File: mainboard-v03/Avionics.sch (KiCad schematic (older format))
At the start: 42 parts, among them J10 Conn_01x03, J8 Conn_01x09, J9 Conn_01x05, SW1 KMR231NG LFS, U1 MAX706RS-T, U2 ATSAMD51J20A-AU, U3 LSM9DS1, Y1 32.768kHz

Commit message: schematic organizing
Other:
- moved on the sheet: J10, J8, J9
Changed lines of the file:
@@
 Text GLabel 4600 5850 0    50   BiDi ~ 0
 PA19
-Text GLabel 1500 5150 2    59   BiDi ~ 0
+Text GLabel 10050 1600 2    59   BiDi ~ 0
 MOSI
-Text GLabel 1500 5050 2    59   BiDi ~ 0
+Text GLabel 10050 1500 2    59   BiDi ~ 0
 SCK
-Text GLabel 1500 5250 2    59   BiDi ~ 0
+Text GLabel 10050 1700 2    59   BiDi ~ 0
 MISO
 Wire Wire Line
-	1500 5150 1400 5150
-Wire Wire Line
-	1500 5050 1400 5050
-Wire Wire Line
-	1500 5250 1400 5250
+	10050 1600 9950 1600
+Wire Wire Line
+	10050 1500 9950 1500
+Wire Wire Line
+	10050 1700 9950 1700
 Wire Wire Line
 	6050 4850 5900 4850
@@
 	3350 1300 3150 1300
 Wire Wire Line
-	1400 5550 1500 5550
-Text GLabel 1500 5550 2    50   BiDi ~ 0
+	9950 2000 10050 2000
+Text GLabel 10050 2000 2    50   BiDi ~ 0
 PA20
 Wire Wire Line
-	1400 5650 1500 5650
-Text GLabel 1500 5650 2    50   BiDi ~ 0
+	9950 2100 10050 2100
+Text GLabel 10050 2100 2    50   BiDi ~ 0
 PA22
 Wire Wire Line
-	1400 5350 1500 5350
-Text GLabel 1500 5350 2    50   BiDi ~ 0
+	9950 1800 10050 1800
+Text GLabel 10050 1800 2    50   BiDi ~ 0
 PB23
 Wire Wire Line
-	1400 5450 1500 5450
-Text GLabel 1500 5450 2    50   BiDi ~ 0
+	9950 1900 10050 1900
+Text GLabel 10050 1900 2    50   BiDi ~ 0
 PB22
 $Comp
 L Connector_Generic:Conn_01x09 J8
 U 1 1 5D3643AA
-P 1200 5250
-F 0 "J8" H 1118 5775 50  0000 C CNN
-F 1 "Conn_01x09" H 1118 5776 50  0001 C CNN
-F 2 "Connector_PinHeader_2.54mm:PinHeader_1x09_P2.54mm_Vertical" H 1200 5250 50  0001 C CNN
-F 3 "~" H 1200 5250 50  0001 C CNN
-	1    1200 5250
+P 9750 1700
+F 0 "J8" H 9668 2225 50  0000 C CNN
+F 1 "Conn_01x09" H 9668 2226 50  0001 C CNN
+F 2 "Connector_PinHeader_2.54mm:PinHeader_1x09_P2.54mm_Vertical" H 9750 1700 50  0001 C CNN
+F 3 "~" H 9750 1700 50  0001 C CNN
+	1    9750 1700
 	-1   0    0    -1
 $EndComp
@@
 L mainboard:3.3V #SUPPLY?
 U 1 0 5D370A56
-P 1950 4850
+P 10500 1300
 AR Path="/5D370A56" Ref="#SUPPLY?"  Part="1"
 AR Path="/5CEC5A72/5D370A56" Ref="#SUPPLY0111"  Part="1"
-F 0 "#SUPPLY0111" H 1950 4850 50  0001 C CNN
-F 1 "3.3V" H 1910 4990 59  0000 L BNN
-F 2 "" H 1950 4850 50  0001 C CNN
-F 3 "" H 1950 4850 50  0001 C CNN
-	1    1950 4850
+F 0 "#SUPPLY0111" H 10500 1300 50  0001 C CNN
+F 1 "3.3V" H 10460 1440 59  0000 L BNN
+F 2 "" H 10500 1300 50  0001 C CNN
+F 3 "" H 10500 1300 50  0001 C CNN
+	1    10500 1300
 	-1   0    0    -1
 $EndComp
@@
 L mainboard:GND #GND?
 U 1 0 5D3722F9
-P 1950 5050
+P 10500 1500
 AR Path="/5D3722F9" Ref="#GND?"  Part="1"
 AR Path="/5CEC5A72/5D3722F9" Ref="#GND0101"  Part="1"
-F 0 "#GND0101" H 1950 5050 50  0001 C CNN
-F 1 "GND" H 1850 4950 59  0000 L BNN
-F 2 "" H 1950 5050 50  0001 C CNN
-F 3 "" H 1950 5050 50  0001 C CNN
-	1    1950 5050
+F 0 "#GND0101" H 10500 1500 50  0001 C CNN
+F 1 "GND" H 10400 1400 59  0000 L BNN
+F 2 "" H 10500 1500 50  0001 C CNN
+F 3 "" H 10500 1500 50  0001 C CNN
+	1    10500 1500
 	1    0    0    -1
 $EndComp
 Wire Wire Line
-	1400 4950 1950 4950
-Wire Wire Line
-	1950 4850 1400 4850
+	9950 1400 10500 1400
+Wire Wire Line
+	10500 1300 9950 1300
 Wire Wire Line
 	4700 4150 4600 4150
@@
 L Connector_Generic:Conn_01x05 J9
 U 1 1 5D408200
-P 1150 6550
-F 0 "J9" H 1068 6967 50  0000 C CNN
-F 1 "Conn_01x05" V 1068 6876 50  0001 C CNN
-F 2 "Connector_PinHeader_2.54mm:PinHeader_1x05_P2.54mm_Vertical" H 1150 6550 50  0001 C CNN
-F 3 "~" H 1150 6550 50  0001 C CNN
-	1    1150 6550
-	-1   0    0    -1
-$EndComp
-Wire Wire Line
-	1350 6350 1450 6350
-Text GLabel 1450 6350 2    50   BiDi ~ 0
+P 9700 3000
+F 0 "J9" H 9618 3417 50  0000 C CNN
+F 1 "Conn_01x05" V 9618 3326 50  0001 C CNN
+F 2 "Connector_PinHeader_2.54mm:PinHeader_1x05_P2.54mm_Vertical" H 9700 3000 50  0001 C CNN
+F 3 "~" H 9700 3000 50  0001 C CNN
+	1    9700 3000
+	-1   0    0    -1
+$EndComp
+Wire Wire Line
+	9900 2800 10000 2800
+Text GLabel 10000 2800 2    50   BiDi ~ 0
 PB17
 Wire Wire Line
-	1350 6450 1450 6450
-Text GLabel 1450 6450 2    50   BiDi ~ 0
+	9900 2900 10000 2900
+Text GLabel 10000 2900 2    50   BiDi ~ 0
 PB16
 Wire Wire Line
-	1350 6650 1450 6650
-Wire Wire Line
-	1350 6750 1450 6750
-Text GLabel 1450 6750 2    50   BiDi ~ 0
+	9900 3100 10000 3100
+Wire Wire Line
+	9900 3200 10000 3200
+Text GLabel 10000 3200 2    50   BiDi ~ 0
 PA16
 Wire Wire Line
-	1350 6550 1450 6550
+	9900 3000 10000 3000
 $Comp
 L Mechanical:MountingHole_Pad H1
@@
 L Connector_Generic:Conn_01x03 J10
 U 1 1 5D538CE6
-P 1900 6550
-F 0 "J10" H 1818 6775 50  0000 C CNN
-F 1 "Conn_01x03" H 1818 6776 50  0001 C CNN
-F 2 "Connector_PinHeader_2.54mm:PinHeader_1x03_P2.54mm_Vertical" H 1900 6550 50  0001 C CNN
-F 3 "~" H 1900 6550 50  0001 C CNN
-	1    1900 6550
-	-1   0    0    -1
-$EndComp
-Wire Wire Line
-	2100 6450 2150 6450
-Text GLabel 2150 6450 2    50   BiDi ~ 0
+P 10450 3000
+F 0 "J10" H 10368 3225 50  0000 C CNN
+F 1 "Conn_01x03" H 10368 3226 50  0001 C CNN
+F 2 "Connector_PinHeader_2.54mm:PinHeader_1x03_P2.54mm_Vertical" H 10450 3000 50  0001 C CNN
+F 3 "~" H 10450 3000 50  0001 C CNN
+	1    10450 3000
+	-1   0    0    -1
+$EndComp
+Wire Wire Line
+	10650 2900 10700 2900
+Text GLabel 10700 2900 2    50   BiDi ~ 0
 DAC0
 Wire Wire Line
-	2100 6650 2150 6650
-Text GLabel 2150 6650 2    50   BiDi ~ 0
+	10650 3100 10700 3100
+Text GLabel 10700 3100 2    50   BiDi ~ 0
 PB14
 Wire Wire Line
-	2100 6550 2150 6550
-Text GLabel 2150 6550 2    50   BiDi ~ 0
+	10650 3000 10700 3000
+Text GLabel 10700 3000 2    50   BiDi ~ 0
 PB15
 Wire Wire Line
@@
 Text GLabel 6050 5950 2    50   BiDi ~ 0
 PB23
-Text GLabel 1450 6650 2    50   BiDi ~ 0
+Text GLabel 10000 3100 2    50   BiDi ~ 0
 PA18
-Text GLabel 1450 6550 2    50   BiDi ~ 0
+Text GLabel 10000 3000 2    50   BiDi ~ 0
 PA19
 Wire Wire Line

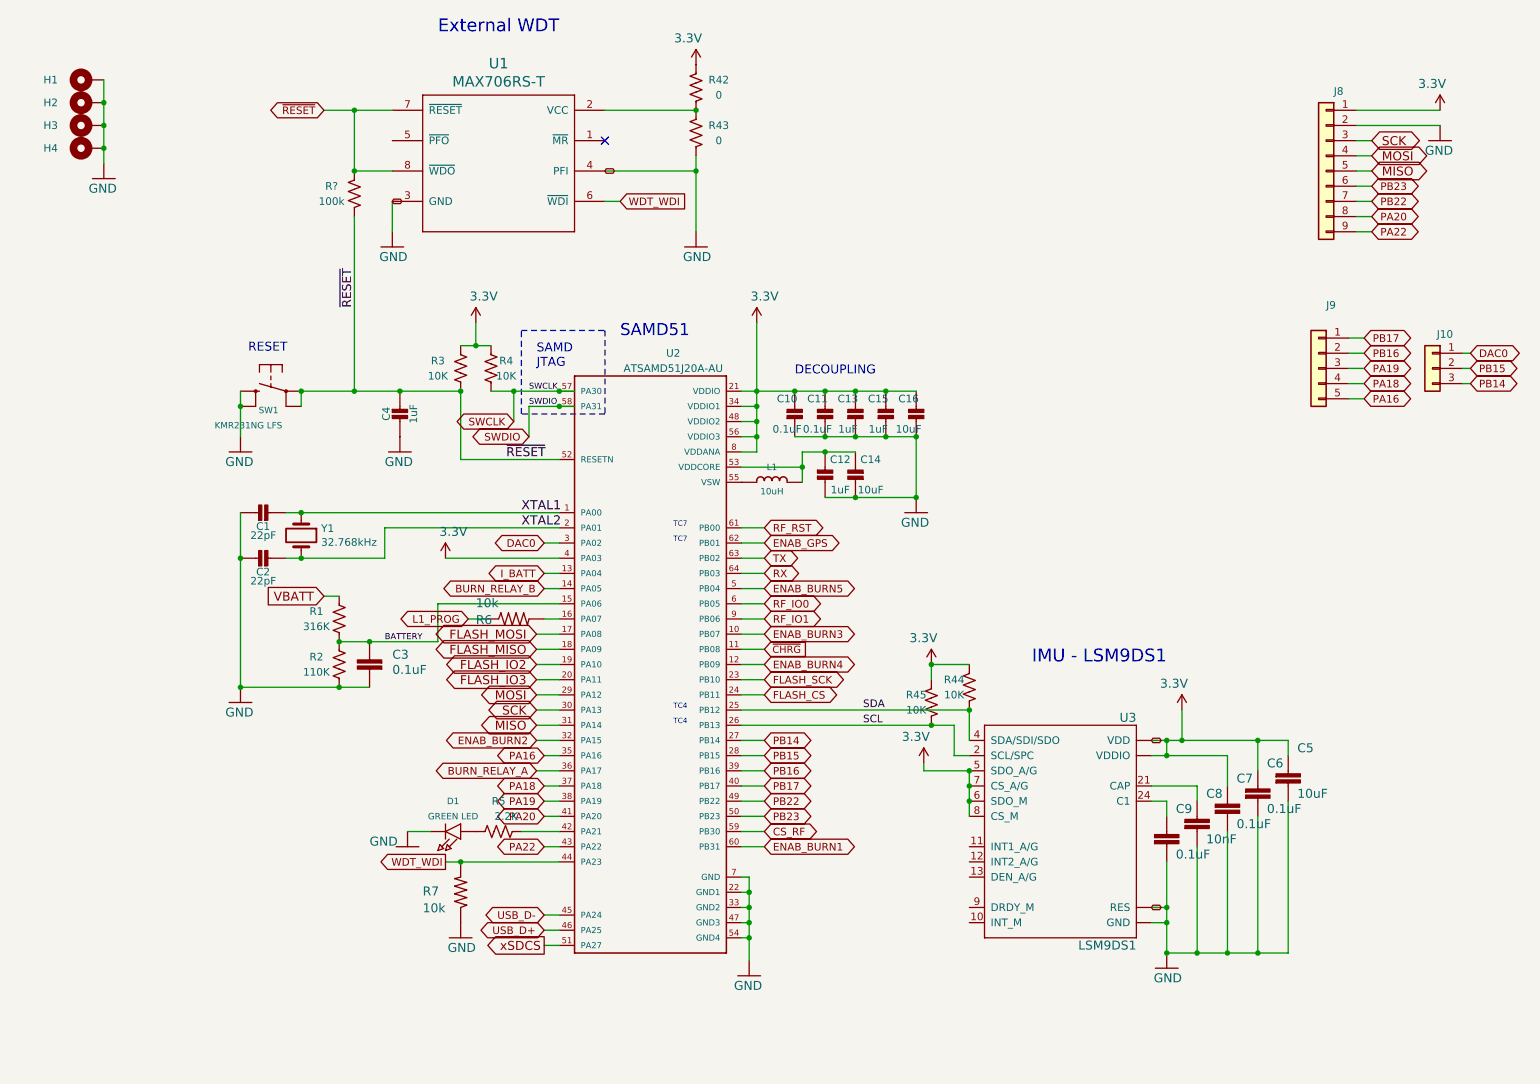
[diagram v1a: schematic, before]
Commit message: cleaning up schematic scheets
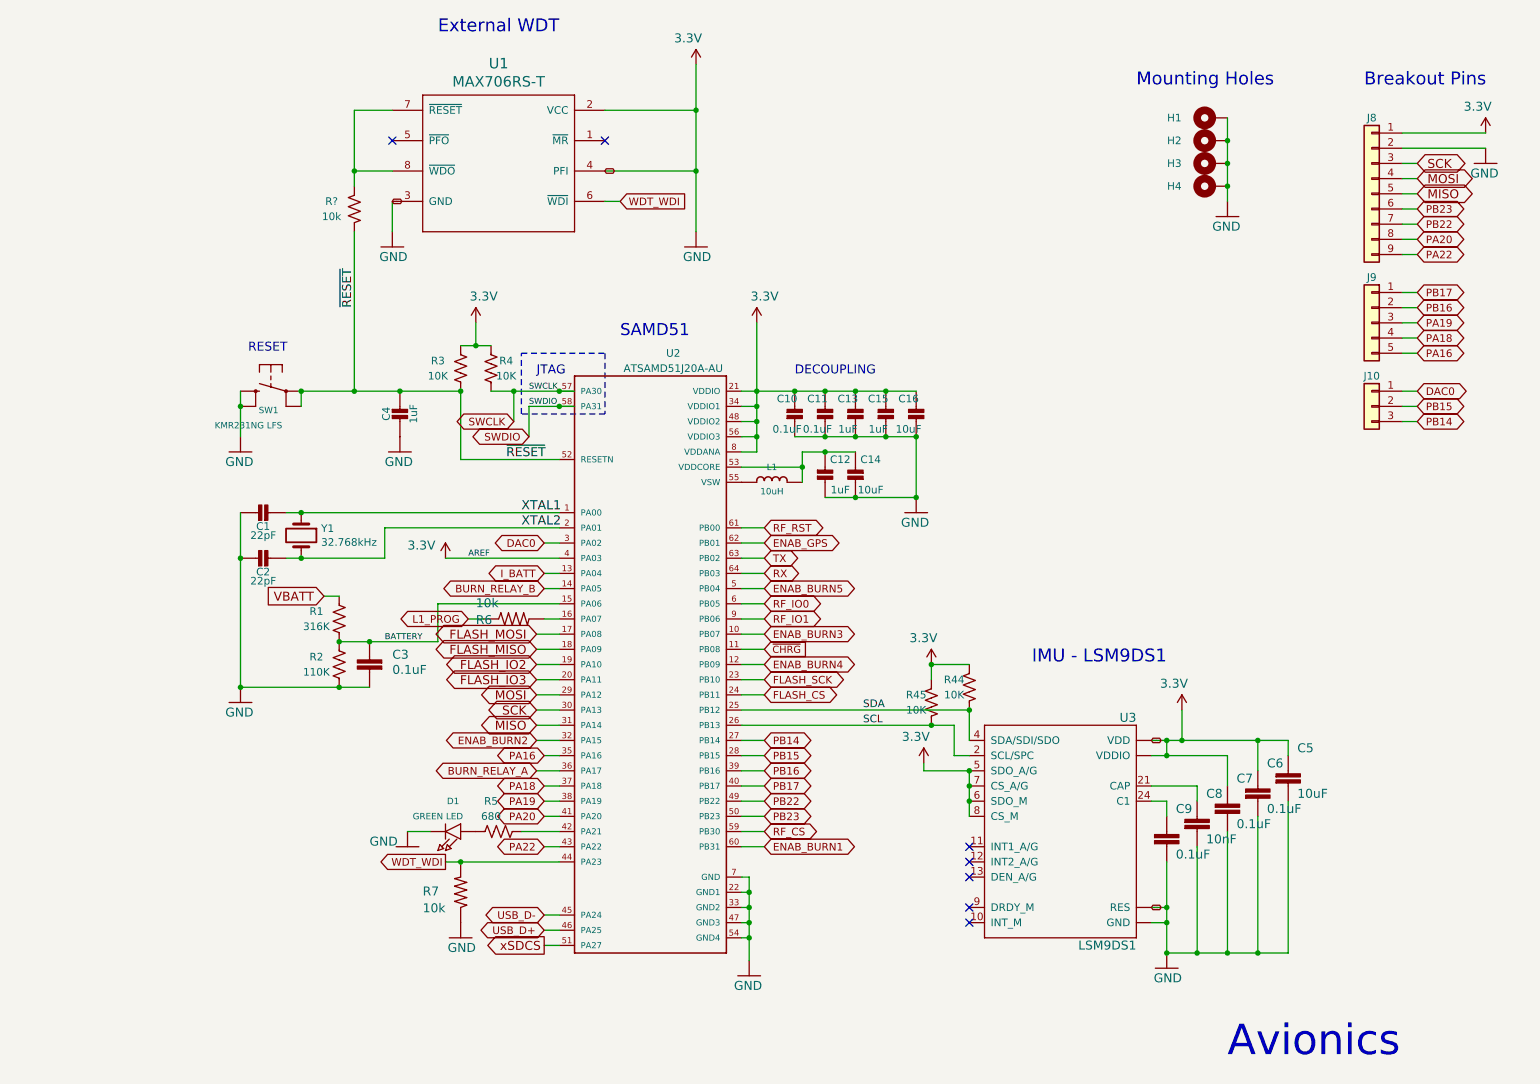
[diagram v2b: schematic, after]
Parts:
- removed R42, R43: 0, Resistor_SMD:R_0603_1608Metric, symbol Device:R_US
- R5: value 2.2K -> 680
- R?: value 100k -> 10k
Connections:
- net GND: now also U1.2 (VCC)
- net ~RESET: no longer R?.2, U1.7 (~RESET), U1.8 (~WDO)
- net AREF: now reaches U2.4 (PA03)
- net CS_RF renamed RF_CS
- new net: R?.2, U1.7 (~RESET), U1.8 (~WDO)
- no-connect marks 1 -> 7
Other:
- note added: "Avionics"
- note added: "Breakout Pins"
- note added: "JTAG\n"
- note added: "Mounting Holes"
- note removed: "SAMD\nJTAG\n"
- note removed: "TC4"
- note removed: "TC7"
- moved on the sheet: H1, H2, H3, H4, J10, J8, J9, R?

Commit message: mainboardv3 clean up
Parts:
- removed J10: Conn_01x03, Connector_PinHeader_2.54mm:PinHeader_1x03_P2.54mm_Vertical, symbol Connector_Generic:Conn_01x03
- added J10: Conn_01x05, Connector_PinHeader_2.54mm:PinHeader_1x05_P2.54mm_Vertical, symbol Connector_Generic:Conn_01x05
- R5: value 680 -> 1K
- U2: footprint QFP50P1200X1200X120-64N -> custom-footprints:QFP50P1200X1200X120-64N
- U3: footprint kmb-test:LGA24-8X4 -> custom-footprints:LSM9DS1
- gave numbers to parts that had none: 1
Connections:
- net PB15 is gone; now on net BURN_RELAY_A: U2.28 (PB15)
- net BURN_RELAY_A: no longer U2.36 (PA17)
- net DAC0: now also J10.1 (Pin_1)
- net GND: no longer U1.2 (VCC)
- net BURN_RELAY_B renamed AIN5
- net AIN5: now also J10.3 (Pin_3)
- net ENAB_BURN3 renamed RF2_BUSY
- net ENAB_BURN4 renamed RF2_CS
- net ENAB_BURN5 renamed RF1_IO4
- net I_BATT renamed AIN4
- net AIN4: now also J10.2 (Pin_2)
- net PA16: no longer names the net of U2.35 (PA16)
- net PA16: no longer J9.5 (Pin_5)
- net PB14 renamed RF2_RST
- net RF_CS renamed RF1_CS
- net RF_IO0 renamed RF1_IO0
- net RF_IO1 renamed RF2_IO1
- net RF_RST renamed RF1_RST
- new net PA17: J9.5 (Pin_5), U2.36 (PA17)
